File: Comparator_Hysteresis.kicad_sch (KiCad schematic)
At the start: 9 parts, among them U8 LMH6611

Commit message: Avance
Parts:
- removed U8: LMH6611, Package_TO_SOT_SMD:TSOT-23-6, symbol Amplifier_Operational:LMH6611
- added D?: BAT54S, Package_TO_SOT_SMD:SOT-23, symbol Diode:BAT54S
- added R?: 10k, symbol 1-Resistor:R
- added U?: TLV9101, LIB_PCB_CONT:SC70-5_TexasInstruments, symbol LIB_SCH_CONTR:TLV9101
- C?: renamed from C37; value 10nF -> 100nF/50V
- R?: renamed from R40; value 11.1K -> 30k
- R?: renamed from R37; value 330R -> 510R
- R?: renamed from R41; value 56.4K -> 100k
- R?: renamed from R39; value 56K -> 100k
- R?: renamed from R38; value 10K -> 510R
- R?: renamed from R42; value 470R -> 2k2
- renumbered D7 to D?
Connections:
- net +3.3V is gone; now on net VDD_OP: R?.1
- net GND: now also D?.1 (A), U?.2 (V-)
- net IN_NAMUR: no longer R?.1
- net OUT_FILTER: now also U?.4
- net VDD_OP: now also C?.1, D?.2 (K), U?.5 (V+)
- net at R?.1, R?.2: now also R?.1, U?.1 (+)
- new net: D?.3 (COM), R?.2, U?.3 (-)
- new net: R?.1, R?.1, R?.2
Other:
- note removed: "tlv2372"
- note removed: "tlv9051 5v"
- note removed: "tlv9104"
- moved on the sheet: C?, D?, R?

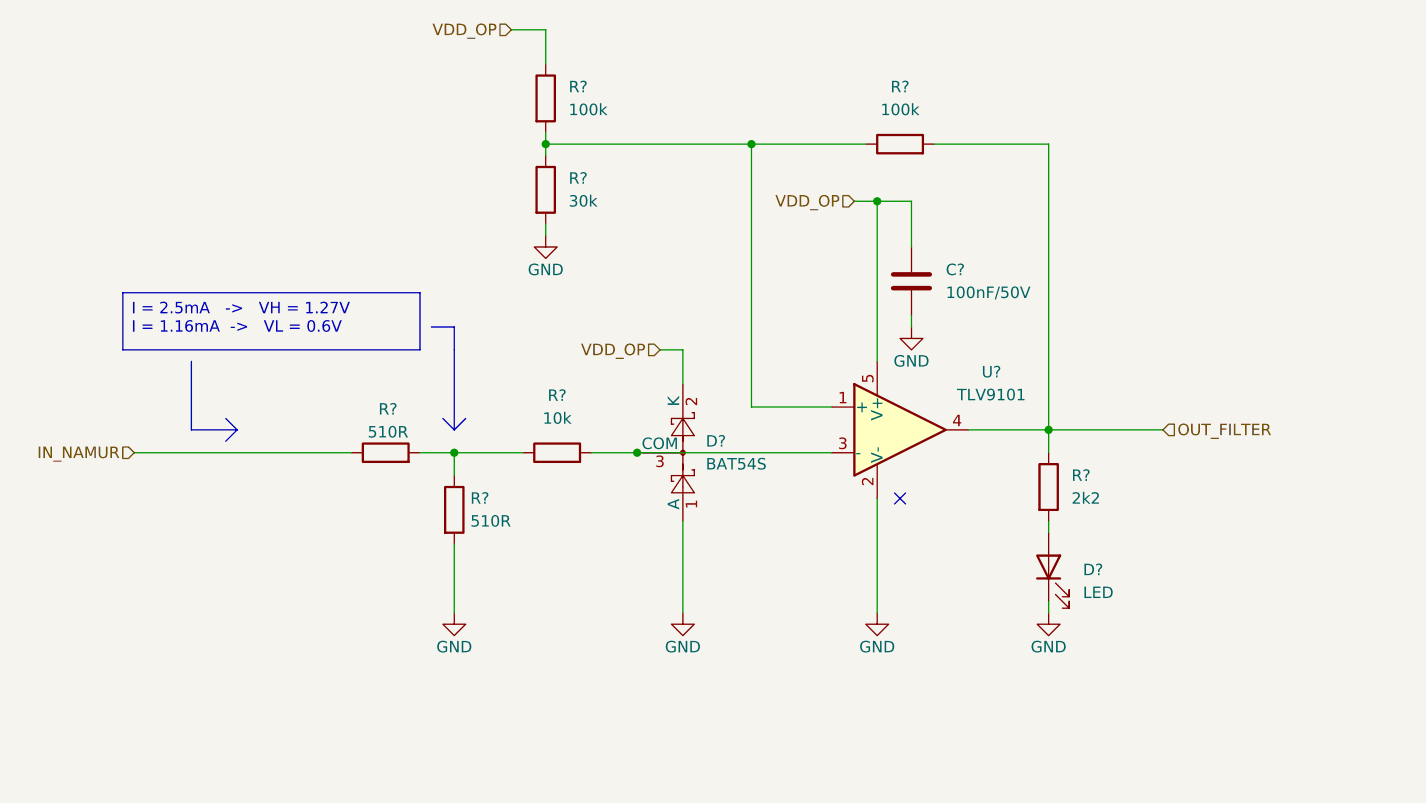
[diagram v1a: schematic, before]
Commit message: avance de pcb, se considera borneras externas para conexión de alimentación
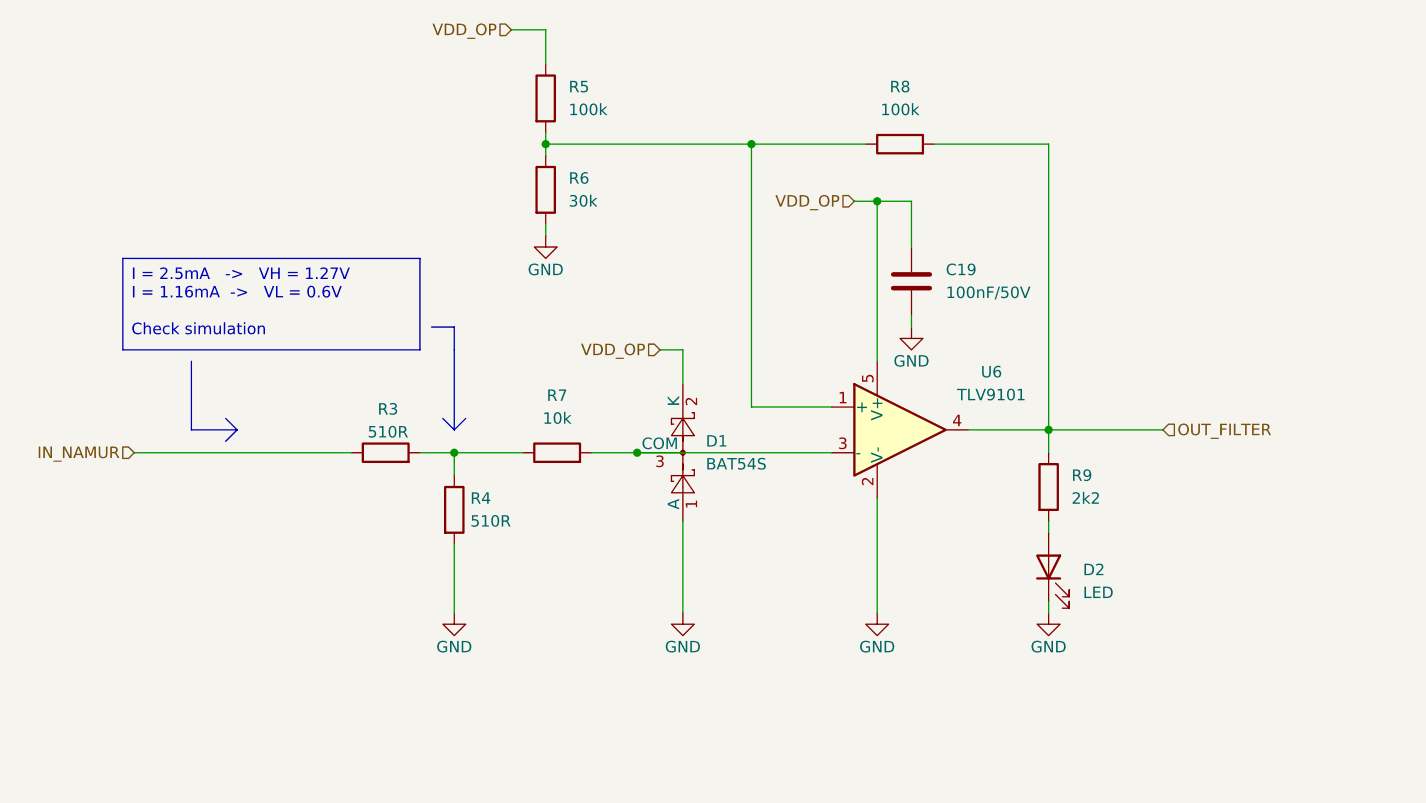
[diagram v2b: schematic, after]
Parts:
- C19: renamed from C?; footprint (none) -> Capacitor_SMD:C_0603_1608Metric
- D2: renamed from D?; footprint (none) -> LED_SMD:LED_0603_1608Metric
- R3, R4, R5, R6, R7, R8, R9: renamed from R?; footprint (none) -> Resistor_SMD:R_0603_1608Metric
- gave numbers to parts that had none: 2
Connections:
- no-connect marks 1 -> 0

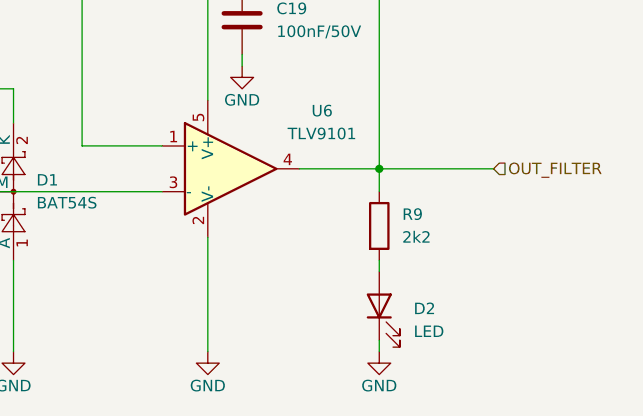
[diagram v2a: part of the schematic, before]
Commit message: Se traza vcc, digital, analog, relay, esta por terminar corregir GND y revisar nuevamente
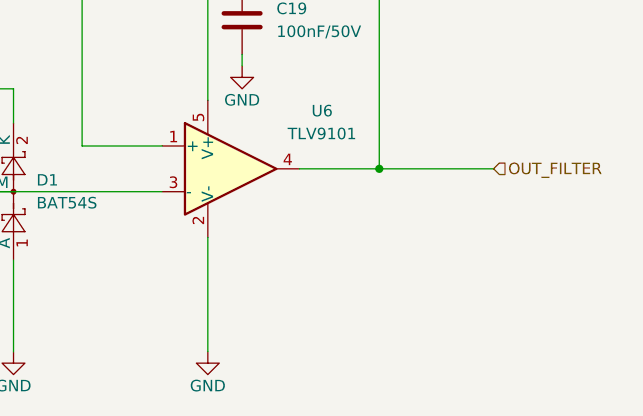
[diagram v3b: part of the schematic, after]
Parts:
- removed D2: LED, LED_SMD:LED_0603_1608Metric, symbol Device:LED
- removed R9: 2k2, Resistor_SMD:R_0603_1608Metric, symbol 1-Resistor:R

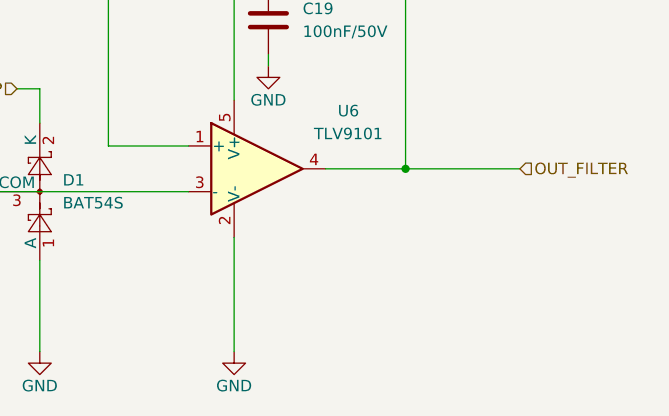
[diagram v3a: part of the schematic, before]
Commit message: Se añaden leds a la entrada de los Namur. Se estandariza y revisan varios footprints de los capacitores. El cambio no fue demasiado, se corrigio en placa. Se hacen algunos cambios adicionales a los valores. Se realiza un avance para jlcpcb
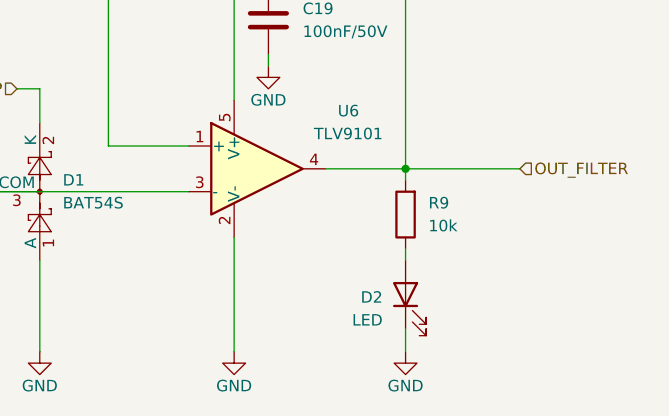
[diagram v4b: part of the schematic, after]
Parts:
- added D2: LED, LED_SMD:LED_0805_2012Metric, symbol Device:LED
- added R9: 10k, Resistor_SMD:R_0603_1608Metric, symbol 1-Resistor:R
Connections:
- net GND: now also D2.1 (K)
- net OUT_FILTER: now also R9.2
- new net: D2.2 (A), R9.1

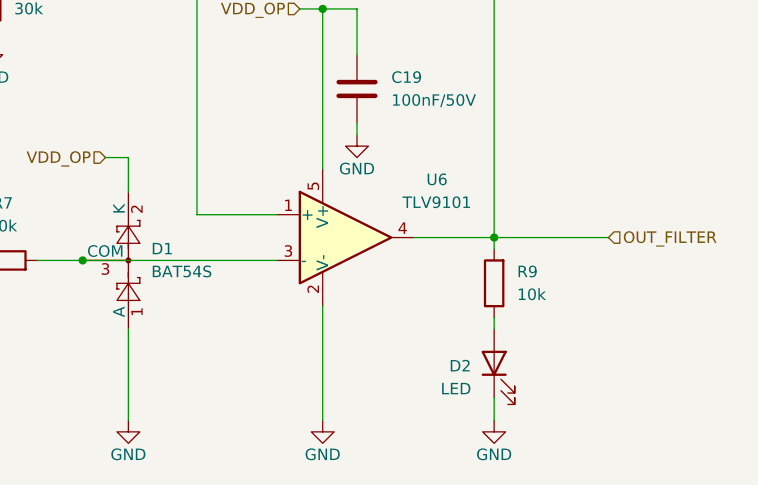
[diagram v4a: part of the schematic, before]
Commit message: Se añade led de status y eeprom externa. Se actualiza pcb y se añade serigrafía adicional. Se actualiza los componentes jlcpcb, se utiliza un micro con con 512kbytes de flash a recomendacion de jefry debido a la escasez de los de 1024 kbytes. Se revisa y se espera mandar a china
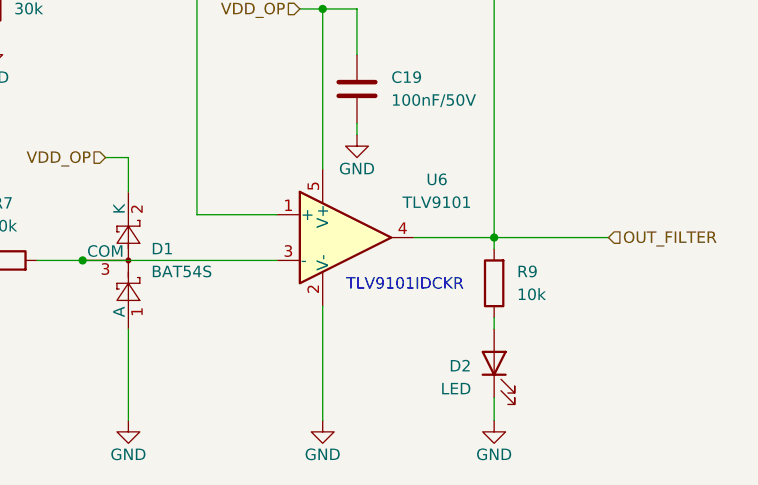
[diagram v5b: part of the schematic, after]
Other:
- note added: "TLV9101IDCKR"
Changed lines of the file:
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@@
 	(generator_version "9.0")
 	(paper "A4")
+	(text "TLV9101IDCKR"
+		(exclude_from_sim no)
+		(at 145.034 90.424 0)
+		(effects
+			(font
+				(size 1.27 1.27)
+			)
+		)
+	)
 	(text_box "I = 2.5mA   ->   VH = 1.27V\nI = 1.16mA  ->   VL = 0.6V \n\nCheck simulation"
 		(exclude_from_sim no)
